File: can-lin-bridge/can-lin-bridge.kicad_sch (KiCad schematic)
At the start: 22 parts, among them IC1 PIC18F26Q83T-I_5N, J1 ICSP, J2 PWR, J3 CAN, J4 LIN, U1 TJA1029TK/20/1J, U2 TJA1042TK/3/2Z

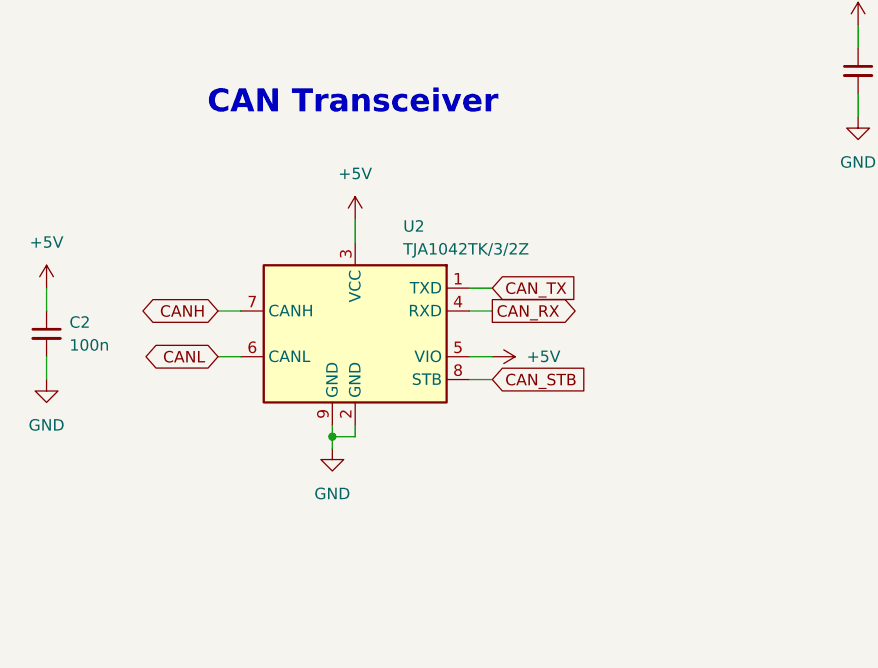
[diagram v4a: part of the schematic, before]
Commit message: can-lin-bridge: Add optional 120 Ohm resistor to CAN bus lines
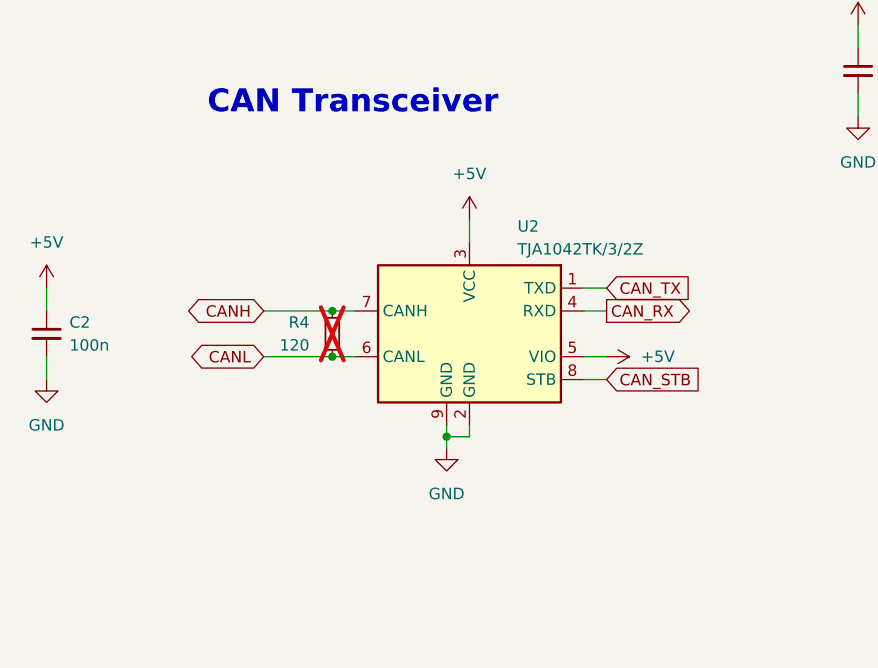
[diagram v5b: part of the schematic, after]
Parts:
- added R4: 120, Resistor_SMD:R_0402_1005Metric, symbol Device:R_Small
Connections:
- net CANH: now also R4.1
- net CANL: now also R4.2
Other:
- moved on the sheet: U2
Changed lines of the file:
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@@
 	)
 	(junction
+		(at 54.61 99.06)
+		(diameter 0)
+		(color 0 0 0 0)
+	)
+	(junction
 		(at 242.57 106.68)
 		(diameter 0)
@@
 	)
 	(junction
-		(at 54.61 107.95)
+		(at 54.61 93.98)
+		(diameter 0)
+		(color 0 0 0 0)
+	)
+	(junction
+		(at 67.31 107.95)
 		(diameter 0)
 		(color 0 0 0 0)
@@
 	(wire
 		(pts
-			(xy 69.85 91.44) (xy 72.39 91.44)
+			(xy 82.55 91.44) (xy 85.09 91.44)
 		)
 		(stroke
@@
 	(wire
 		(pts
-			(xy 54.61 107.95) (xy 57.15 107.95)
+			(xy 67.31 107.95) (xy 69.85 107.95)
 		)
 		(stroke
@@
 	(wire
 		(pts
+			(xy 54.61 93.98) (xy 57.15 93.98)
+		)
+		(stroke
+			(width 0)
+			(type default)
+		)
+	)
+	(wire
+		(pts
 			(xy 242.57 105.41) (xy 242.57 106.68)
 		)
@@
 	(wire
 		(pts
-			(xy 54.61 106.68) (xy 54.61 107.95)
+			(xy 67.31 106.68) (xy 67.31 107.95)
 		)
 		(stroke
@@
 	(wire
 		(pts
-			(xy 57.15 106.68) (xy 57.15 107.95)
+			(xy 69.85 106.68) (xy 69.85 107.95)
 		)
 		(stroke
@@
 	(wire
 		(pts
-			(xy 41.91 93.98) (xy 44.45 93.98)
+			(xy 46.99 93.98) (xy 54.61 93.98)
 		)
 		(stroke
@@
 	(wire
 		(pts
-			(xy 57.15 83.82) (xy 57.15 86.36)
+			(xy 69.85 83.82) (xy 69.85 86.36)
 		)
 		(stroke
@@
 	(wire
 		(pts
-			(xy 54.61 107.95) (xy 54.61 109.22)
+			(xy 67.31 107.95) (xy 67.31 109.22)
 		)
 		(stroke
@@
 	(wire
 		(pts
-			(xy 69.85 99.06) (xy 72.39 99.06)
+			(xy 82.55 99.06) (xy 85.09 99.06)
 		)
 		(stroke
@@
 	(wire
 		(pts
-			(xy 69.85 101.6) (xy 72.39 101.6)
+			(xy 82.55 101.6) (xy 85.09 101.6)
 		)
 		(stroke
@@
 	(wire
 		(pts
-			(xy 41.91 99.06) (xy 44.45 99.06)
+			(xy 46.99 99.06) (xy 54.61 99.06)
 		)
 		(stroke
@@
 	(wire
 		(pts
-			(xy 69.85 93.98) (xy 72.39 93.98)
+			(xy 54.61 99.06) (xy 57.15 99.06)
+		)
+		(stroke
+			(width 0)
+			(type default)
+		)
+	)
+	(wire
+		(pts
+			(xy 82.55 93.98) (xy 85.09 93.98)
 		)
 		(stroke
@@
 	(global_label "CAN_STB"
 		(shape input)
-		(at 72.39 101.6 0)
+		(at 85.09 101.6 0)
 		(fields_autoplaced yes)
 		(effects
@@
 		)
 		(property "Intersheetrefs" "${INTERSHEET_REFS}"
-			(at 83.479 101.6 0)
+			(at 96.179 101.6 0)
 			(effects
 				(font
@@
 	(global_label "CAN_RX"
 		(shape output)
-		(at 72.39 93.98 0)
+		(at 85.09 93.98 0)
 		(fields_autoplaced yes)
 		(effects
@@
 		)
 		(property "Intersheetrefs" "${INTERSHEET_REFS}"
-			(at 82.5114 93.98 0)
+			(at 95.2114 93.98 0)
 			(effects
 				(font
@@
 	(global_label "CANL"
 		(shape bidirectional)
-		(at 41.91 99.06 180)
+		(at 46.99 99.06 180)
 		(fields_autoplaced yes)
 		(effects
@@
 		)
 		(property "Intersheetrefs" "${INTERSHEET_REFS}"
-			(at 33.0963 99.06 0)
+			(at 38.1763 99.06 0)
 			(effects
 				(font
@@
 	(global_label "CAN_TX"
 		(shape input)
-		(at 72.39 91.44 0)
+		(at 85.09 91.44 0)
 		(fields_autoplaced yes)
 		(effects
@@
 		)
 		(property "Intersheetrefs" "${INTERSHEET_REFS}"
-			(at 82.209 91.44 0)
+			(at 94.909 91.44 0)
 			(effects
 				(font
@@
 	(global_label "CANH"
 		(shape bidirectional)
-		(at 41.91 93.98 180)
+		(at 46.99 93.98 180)
 		(fields_autoplaced yes)
 		(effects
@@
 		)
 		(property "Intersheetrefs" "${INTERSHEET_REFS}"
-			(at 32.7939 93.98 0)
+			(at 37.8739 93.98 0)
 			(effects
 				(font
@@
 	(symbol
 		(lib_id "power:+5V")
-		(at 72.39 99.06 270)
+		(at 85.09 99.06 270)
 		(unit 1)
 		(exclude_from_sim no)
@@
 		(fields_autoplaced yes)
 		(property "Reference" "#PWR05"
-			(at 68.58 99.06 0)
+			(at 81.28 99.06 0)
 			(effects
 				(font
@@
 		)
 		(property "Value" "+5V"
-			(at 76.2 99.0599 90)
+			(at 88.9 99.0599 90)
 			(effects
 				(font
@@
 		)
 		(property "Footprint" ""
-			(at 72.39 99.06 0)
+			(at 85.09 99.06 0)
 			(effects
 				(font
@@
 		)
 		(property "Datasheet" ""
-			(at 72.39 99.06 0)
+			(at 85.09 99.06 0)
 			(effects
 				(font
@@
 		)
 		(property "Description" "Power symbol creates a global label with name \"+5V\""
-			(at 72.39 99.06 0)
+			(at 85.09 99.06 0)
 			(effects
 				(font
@@
 	(symbol
 		(lib_id "Interface_CAN_LIN:TJA1042TK-3")
-		(at 57.15 96.52 0)
+		(at 69.85 96.52 0)
 		(mirror y)
 		(unit 1)
@@
 		(dnp no)
 		(property "Reference" "U2"
-			(at 62.484 84.582 0)
+			(at 75.184 84.582 0)
 			(effects
 				(font
@@
 		)
 		(property "Value" "TJA1042TK/3/2Z"
-			(at 62.484 87.122 0)
+			(at 75.184 87.122 0)
 			(effects
 				(font
@@
 		)
 		(property "Footprint" "Package_DFN_QFN:DFN-8-1EP_3x3mm_P0.65mm_EP1.55x2.4mm"
-			(at 57.15 109.22 0)
+			(at 69.85 109.22 0)
 			(effects
 				(font
@@
 		)
 		(property "Datasheet" "http://www.nxp.com/docs/en/data-sheet/TJA1042.pdf"
-			(at 57.15 96.52 0)
+			(at 69.85 96.52 0)
 			(effects
 				(font
@@
 		)
 		(property "Description" "High-Speed CAN Transceiver, separate VIO, standby mode, DFN-8-1EP"
-			(at 57.15 96.52 0)
+			(at 69.85 96.52 0)
 			(effects
 				(font
@@
 	)
 	(symbol
+		(lib_id "Device:R_Small")
+		(at 54.61 96.52 0)
+		(mirror y)
+		(unit 1)
+		(exclude_from_sim no)
+		(in_bom yes)
+		(on_board yes)
+		(dnp yes)
+		(property "Reference" "R4"
+			(at 52.07 95.2499 0)
+			(effects
+				(font
+					(size 1.27 1.27)
+				)
+				(justify left)
+			)
+		)
+		(property "Value" "120"
+			(at 52.07 97.7899 0)
+			(effects
+				(font
+					(size 1.27 1.27)
+				)
+				(justify left)
+			)
+		)
+		(property "Footprint" "Resistor_SMD:R_0402_1005Metric"
+			(at 54.61 96.52 0)
+			(effects
+				(font
+					(size 1.27 1.27)
+				)
+				(hide yes)
+			)
+		)
+		(property "Datasheet" "~"
+			(at 54.61 96.52 0)
+			(effects
+				(font
+					(size 1.27 1.27)
+				)
+				(hide yes)
+			)
+		)
+		(property "Description" "Resistor, small symbol"
+			(at 54.61 96.52 0)
+			(effects
+				(font
+					(size 1.27 1.27)
+				)
+				(hide yes)
+			)
+		)
+		(pin "1"
+		)
+		(pin "2"
+		)
+		(instances
+			(project ""
+				(path "/d5aaab65-b0a5-472e-8b3a-9378b5d7faec"
+					(reference "R4")
+					(unit 1)
+				)
+			)
+		)
+	)
+	(symbol
 		(lib_id "power:+5V")
 		(at 140.97 63.5 0)
@@
 	(symbol
 		(lib_id "power:+5V")
-		(at 57.15 83.82 0)
+		(at 69.85 83.82 0)
 		(unit 1)
 		(exclude_from_sim no)
@@
 		(fields_autoplaced yes)
 		(property "Reference" "#PWR04"
-			(at 57.15 87.63 0)
+			(at 69.85 87.63 0)
 			(effects
 				(font
@@
 		)
 		(property "Value" "+5V"
-			(at 57.15 78.74 0)
+			(at 69.85 78.74 0)
 			(effects
 				(font
@@
 		)
 		(property "Footprint" ""
-			(at 57.15 83.82 0)
+			(at 69.85 83.82 0)
 			(effects
 				(font
@@
 		)
 		(property "Datasheet" ""
-			(at 57.15 83.82 0)
+			(at 69.85 83.82 0)
 			(effects
 				(font
@@
 		)
 		(property "Description" "Power symbol creates a global label with name \"+5V\""
-			(at 57.15 83.82 0)
+			(at 69.85 83.82 0)
 			(effects
 				(font
@@
 	(symbol
 		(lib_id "power:GND")
-		(at 54.61 109.22 0)
+		(at 67.31 109.22 0)
 		(unit 1)
 		(exclude_from_sim no)
@@
 		(fields_autoplaced yes)
 		(property "Reference" "#PWR03"
-			(at 54.61 115.57 0)
+			(at 67.31 115.57 0)
 			(effects
 				(font
@@
 		)
 		(property "Value" "GND"
-			(at 54.61 114.3 0)
+			(at 67.31 114.3 0)
 			(effects
 				(font
@@
 		)
 		(property "Footprint" ""
-			(at 54.61 109.22 0)
+			(at 67.31 109.22 0)
 			(effects
 				(font
@@
 		)
 		(property "Datasheet" ""
-			(at 54.61 109.22 0)
+			(at 67.31 109.22 0)
 			(effects
 				(font
@@
 		)
 		(property "Description" "Power symbol creates a global label with name \"GND\" , ground"
-			(at 54.61 109.22 0)
+			(at 67.31 109.22 0)
 			(effects
 				(font

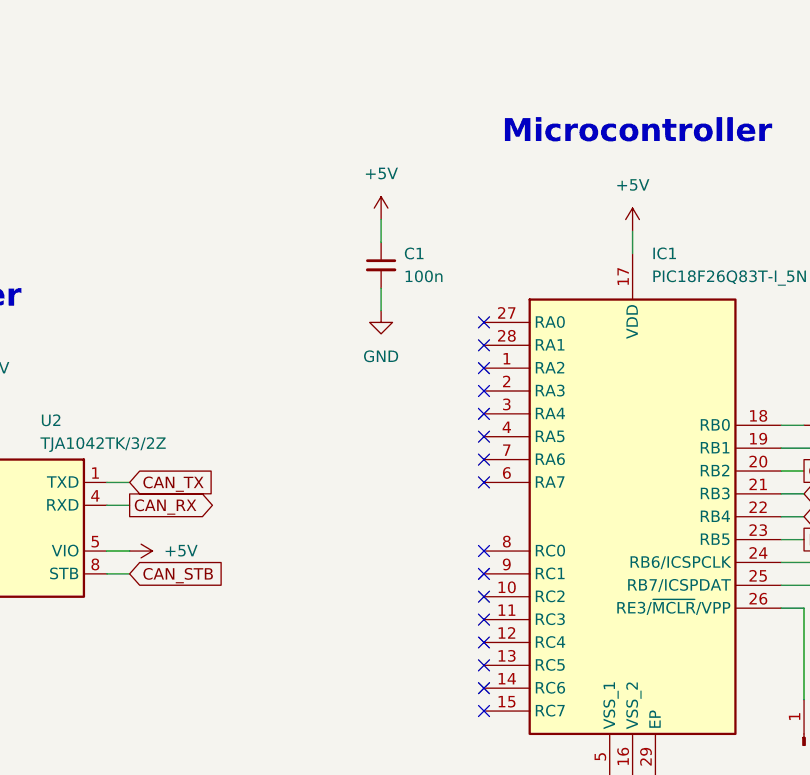
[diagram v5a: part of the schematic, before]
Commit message: can-lin-bridge: Connect LIN sleep and CAN standby pins to microcontroller
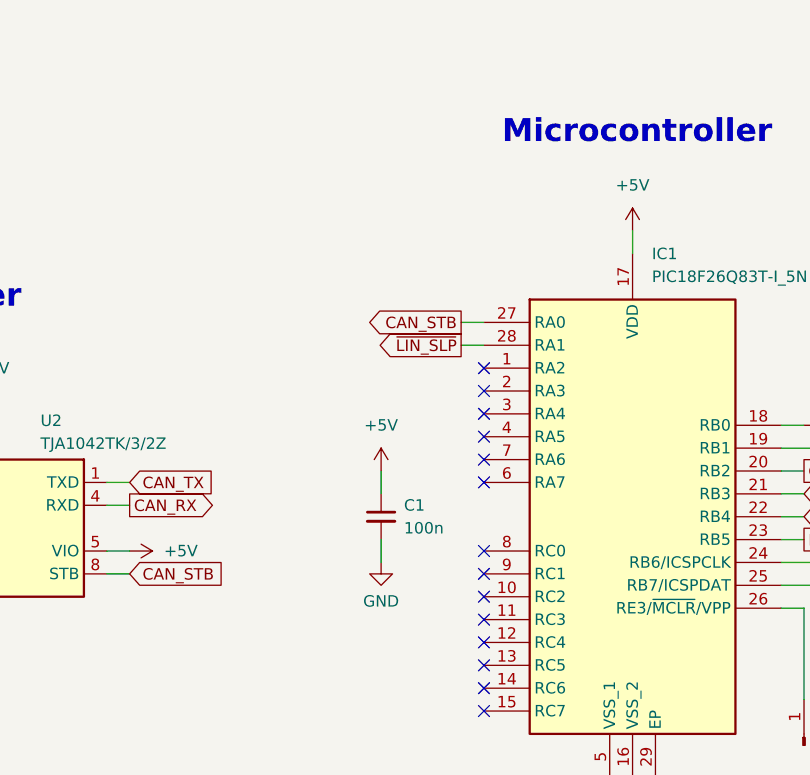
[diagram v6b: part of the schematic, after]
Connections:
- net CAN_STB: now also IC1.27 (RA0)
- net ~{LIN_SLP}: now also IC1.28 (RA1)
- no-connect marks 16 -> 14
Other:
- moved on the sheet: C1
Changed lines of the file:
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@@
+	)
+	(no_connect
+		(at 124.46 116.84)
 	)
 	(no_connect
@@
 	)
 	(no_connect
-		(at 124.46 114.3)
-	)
-	(no_connect
 		(at 124.46 99.06)
 	)
@@
 	)
 	(no_connect
-		(at 124.46 73.66)
+		(at 124.46 101.6)
 	)
 	(no_connect
-		(at 124.46 116.84)
-	)
-	(no_connect
-		(at 124.46 101.6)
-	)
-	(no_connect
-		(at 124.46 76.2)
+		(at 124.46 114.3)
 	)
 	(no_connect
@@
 	(wire
 		(pts
+			(xy 121.92 76.2) (xy 124.46 76.2)
+		)
+		(stroke
+			(width 0)
+			(type default)
+		)
+	)
+	(wire
+		(pts
 			(xy 67.31 107.95) (xy 69.85 107.95)
 		)
@@
 	(wire
 		(pts
-			(xy 113.03 62.23) (xy 113.03 64.77)
+			(xy 113.03 90.17) (xy 113.03 92.71)
 		)
 		(stroke
@@
 	(wire
 		(pts
-			(xy 113.03 69.85) (xy 113.03 72.39)
+			(xy 113.03 97.79) (xy 113.03 100.33)
 		)
 		(stroke
@@
 		(pts
 			(xy 160.02 105.41) (xy 157.48 105.41)
+		)
+		(stroke
+			(width 0)
+			(type default)
+		)
+	)
+	(wire
+		(pts
+			(xy 121.92 73.66) (xy 124.46 73.66)
 		)
 		(stroke
@@
 		)
 	)
+	(global_label "CAN_STB"
+		(shape output)
+		(at 121.92 73.66 180)
+		(fields_autoplaced yes)
+		(effects
+			(font
+				(size 1.27 1.27)
+			)
+			(justify right)
+		)
+		(property "Intersheetrefs" "${INTERSHEET_REFS}"
+			(at 110.831 73.66 0)
+			(effects
+				(font
+					(size 1.27 1.27)
+				)
+				(justify right)
+				(hide yes)
+			)
+		)
+	)
 	(global_label "~{LIN_SLP}"
 		(shape input)
@@
 				)
 				(justify left)
+				(hide yes)
+			)
+		)
+	)
+	(global_label "~{LIN_SLP}"
+		(shape output)
+		(at 121.92 76.2 180)
+		(fields_autoplaced yes)
+		(effects
+			(font
+				(size 1.27 1.27)
+			)
+			(justify right)
+		)
+		(property "Intersheetrefs" "${INTERSHEET_REFS}"
+			(at 111.4962 76.2 0)
+			(effects
+				(font
+					(size 1.27 1.27)
+				)
+				(justify right)
 				(hide yes)
 			)
@@
 	(symbol
 		(lib_id "power:GND")
-		(at 113.03 72.39 0)
+		(at 113.03 100.33 0)
 		(unit 1)
 		(exclude_from_sim no)
@@
 		(on_board yes)
 		(dnp no)
-		(fields_autoplaced yes)
 		(property "Reference" "#PWR09"
-			(at 113.03 78.74 0)
+			(at 113.03 106.68 0)
 			(effects
 				(font
@@
 		)
 		(property "Value" "GND"
-			(at 113.03 77.47 0)
+			(at 113.03 104.648 0)
 			(effects
 				(font
@@
 		)
 		(property "Footprint" ""
-			(at 113.03 72.39 0)
+			(at 113.03 100.33 0)
 			(effects
 				(font
@@
 		)
 		(property "Datasheet" ""
-			(at 113.03 72.39 0)
+			(at 113.03 100.33 0)
 			(effects
 				(font
@@
 		)
 		(property "Description" "Power symbol creates a global label with name \"GND\" , ground"
-			(at 113.03 72.39 0)
+			(at 113.03 100.33 0)
 			(effects
 				(font
@@
 	(symbol
 		(lib_id "Device:C_Small")
-		(at 113.03 67.31 0)
+		(at 113.03 95.25 0)
 		(unit 1)
 		(exclude_from_sim no)
@@
 		(fields_autoplaced yes)
 		(property "Reference" "C1"
-			(at 115.57 66.0462 0)
+			(at 115.57 93.9862 0)
 			(effects
 				(font
@@
 		)
 		(property "Value" "100n"
-			(at 115.57 68.5862 0)
+			(at 115.57 96.5262 0)
 			(effects
 				(font
@@
 		)
 		(property "Footprint" "Capacitor_SMD:C_0402_1005Metric"
-			(at 113.03 67.31 0)
+			(at 113.03 95.25 0)
 			(effects
 				(font
@@
 		)
 		(property "Datasheet" "~"
-			(at 113.03 67.31 0)
+			(at 113.03 95.25 0)
 			(effects
 				(font
@@
 		)
 		(property "Description" "Unpolarized capacitor, small symbol"
-			(at 113.03 67.31 0)
+			(at 113.03 95.25 0)
 			(effects
 				(font
@@
 	(symbol
 		(lib_id "power:+5V")
-		(at 113.03 62.23 0)
+		(at 113.03 90.17 0)
 		(unit 1)
 		(exclude_from_sim no)
@@
 		(fields_autoplaced yes)
 		(property "Reference" "#PWR08"
-			(at 113.03 66.04 0)
+			(at 113.03 93.98 0)
 			(effects
 				(font
@@
 		)
 		(property "Value" "+5V"
-			(at 113.03 57.15 0)
+			(at 113.03 85.09 0)
 			(effects
 				(font
@@
 		)
 		(property "Footprint" ""
-			(at 113.03 62.23 0)
+			(at 113.03 90.17 0)
 			(effects
 				(font
@@
 		)
 		(property "Datasheet" ""
-			(at 113.03 62.23 0)
+			(at 113.03 90.17 0)
 			(effects
 				(font
@@
 		)
 		(property "Description" "Power symbol creates a global label with name \"+5V\""
-			(at 113.03 62.23 0)
-			(effects
-				(font
+			(at 113.03 90.17 0)
+			(effects
+				(font

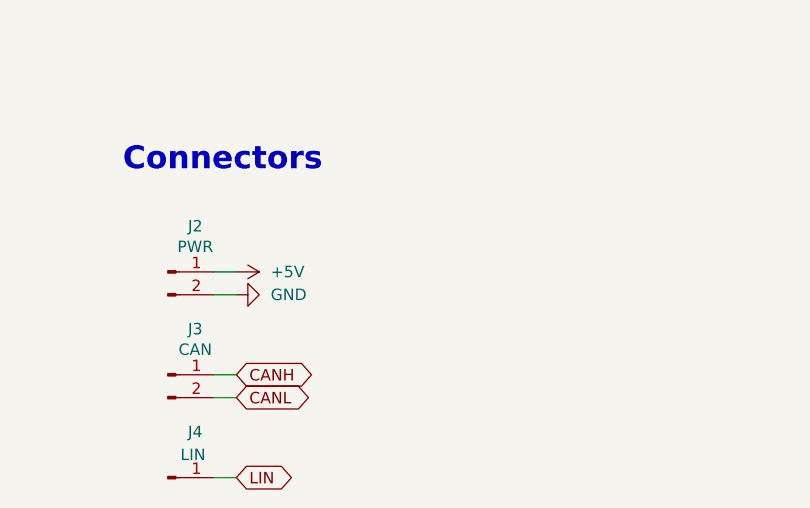
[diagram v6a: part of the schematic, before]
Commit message: can-lin-bridge: Add 4.7 uF tank capacitor
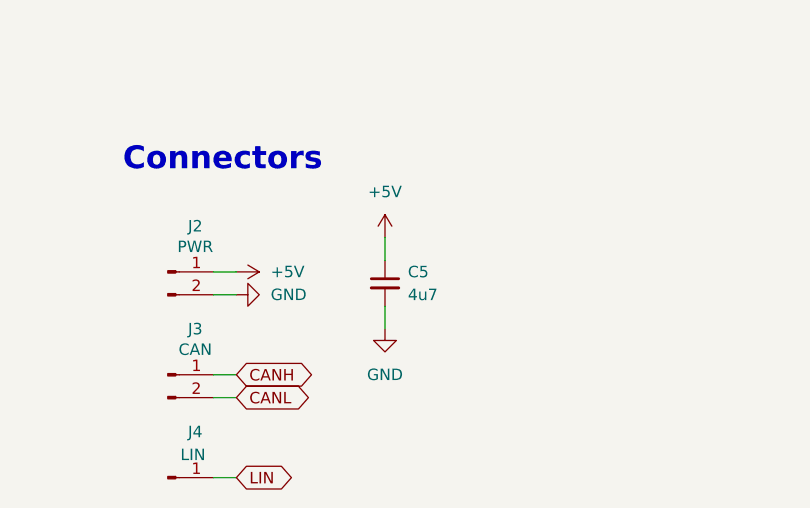
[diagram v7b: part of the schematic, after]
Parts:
- added C5: 4u7, Capacitor_SMD:C_0603_1608Metric, symbol Device:C_Small
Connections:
- net +5V: now also C5.1
- net GND: now also C5.2
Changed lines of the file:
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@@
 	(wire
 		(pts
+			(xy 76.2 147.32) (xy 76.2 149.86)
+		)
+		(stroke
+			(width 0)
+			(type default)
+		)
+	)
+	(wire
+		(pts
 			(xy 113.03 90.17) (xy 113.03 92.71)
 		)
@@
 	(wire
 		(pts
+			(xy 76.2 154.94) (xy 76.2 157.48)
+		)
+		(stroke
+			(width 0)
+			(type default)
+		)
+	)
+	(wire
+		(pts
 			(xy 59.69 29.21) (xy 59.69 31.75)
 		)
@@
 	)
 	(symbol
+		(lib_id "power:GND")
+		(at 76.2 157.48 0)
+		(unit 1)
+		(exclude_from_sim no)
+		(in_bom yes)
+		(on_board yes)
+		(dnp no)
+		(fields_autoplaced yes)
+		(property "Reference" "#PWR023"
+			(at 76.2 163.83 0)
+			(effects
+				(font
+					(size 1.27 1.27)
+				)
+				(hide yes)
+			)
+		)
+		(property "Value" "GND"
+			(at 76.2 162.56 0)
+			(effects
+				(font
+					(size 1.27 1.27)
+				)
+			)
+		)
+		(property "Footprint" ""
+			(at 76.2 157.48 0)
+			(effects
+				(font
+					(size 1.27 1.27)
+				)
+				(hide yes)
+			)
+		)
+		(property "Datasheet" ""
+			(at 76.2 157.48 0)
+			(effects
+				(font
+					(size 1.27 1.27)
+				)
+				(hide yes)
+			)
+		)
+		(property "Description" "Power symbol creates a global label with name \"GND\" , ground"
+			(at 76.2 157.48 0)
+			(effects
+				(font
+					(size 1.27 1.27)
+				)
+				(hide yes)
+			)
+		)
+		(pin "1"
+		)
+		(instances
+			(project "can-lin-bridge"
+				(path "/d5aaab65-b0a5-472e-8b3a-9378b5d7faec"
+					(reference "#PWR023")
+					(unit 1)
+				)
+			)
+		)
+	)
+	(symbol
 		(lib_id "power:+5V")
 		(at 22.86 91.44 0)
@@
 					(unit 1)
 				)
+			)
+		)
+	)
+	(symbol
+		(lib_id "Device:C_Small")
+		(at 76.2 152.4 0)
+		(unit 1)
+		(exclude_from_sim no)
+		(in_bom yes)
+		(on_board yes)
+		(dnp no)
+		(fields_autoplaced yes)
+		(property "Reference" "C5"
+			(at 78.74 151.1362 0)
+			(effects
+				(font
+					(size 1.27 1.27)
+				)
+				(justify left)
+			)
+		)
+		(property "Value" "4u7"
+			(at 78.74 153.6762 0)
+			(effects
+				(font
+					(size 1.27 1.27)
+				)
+				(justify left)
+			)
+		)
+		(property "Footprint" "Capacitor_SMD:C_0603_1608Metric"
+			(at 76.2 152.4 0)
+			(effects
+				(font
+					(size 1.27 1.27)
+				)
+				(hide yes)
+			)
+		)
+		(property "Datasheet" "~"
+			(at 76.2 152.4 0)
+			(effects
+				(font
+					(size 1.27 1.27)
+				)
+				(hide yes)
+			)
+		)
+		(property "Description" "Unpolarized capacitor, small symbol"
+			(at 76.2 152.4 0)
+			(effects
+				(font
+					(size 1.27 1.27)
+				)
+				(hide yes)
+			)
+		)
+		(pin "1"
+		)
+		(pin "2"
+		)
+		(instances
+			(project "can-lin-bridge"
+				(path "/d5aaab65-b0a5-472e-8b3a-9378b5d7faec"
+					(reference "C5")
+					(unit 1)
+				)
+			)
+		)
+	)
+	(symbol
+		(lib_id "power:+5V")
+		(at 76.2 147.32 0)
+		(unit 1)
+		(exclude_from_sim no)
+		(in_bom yes)
+		(on_board yes)
+		(dnp no)
+		(fields_autoplaced yes)
+		(property "Reference" "#PWR022"
+			(at 76.2 151.13 0)
+			(effects
+				(font
+					(size 1.27 1.27)
+				)
+				(hide yes)
+			)
+		)
+		(property "Value" "+5V"
+			(at 76.2 142.24 0)
+			(effects
+				(font
+					(size 1.27 1.27)
+				)
+			)
+		)
+		(property "Footprint" ""
+			(at 76.2 147.32 0)
+			(effects
+				(font
+					(size 1.27 1.27)
+				)
+				(hide yes)
+			)
+		)
+		(property "Datasheet" ""
+			(at 76.2 147.32 0)
+			(effects
+				(font
+					(size 1.27 1.27)
+				)
+				(hide yes)
+			)
+		)
+		(property "Description" "Power symbol creates a global label with name \"+5V\""
+			(at 76.2 147.32 0)
+			(effects
+				(font
+					(size 1.27 1.27)
+				)
+				(hide yes)
+			)
+		)
+		(pin "1"
+		)
+		(instances
+			(project "can-lin-bridge"
+				(path "/d5aaab65-b0a5-472e-8b3a-9378b5d7faec"
+					(reference "#PWR022")
+					(unit 1)
+				)
